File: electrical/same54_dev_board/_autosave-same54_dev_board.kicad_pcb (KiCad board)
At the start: 2 copper layers, 177.8 x 83.8 mm, 7 parts, among them J1 USB_B_Micro, J2 Conn_ARM_JTAG_SWD_10, J3 Conn_02x20_Odd_Even_LCD_INTF, U1 p_ATSAME54P20A-AU, U2 FT232RQ-REEL, U3 MAX7301AAX+, Y1 XOSC32

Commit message: Trying to figure out how I want to do power...
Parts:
- J2: footprint Connector_PinSocket_1.27mm:PinSocket_2x04_P1.27mm_Vertical -> Connector_PinHeader_1.27mm:PinHeader_2x05_P1.27mm_Vertical
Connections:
- net /g_SCREEN_INTF/D0 renamed /s_SCREEN_INTF/D0
- net /g_SCREEN_INTF/D1 renamed /s_SCREEN_INTF/D1
- net /g_SCREEN_INTF/D10 renamed /s_SCREEN_INTF/D10
- net /g_SCREEN_INTF/D11 renamed /s_SCREEN_INTF/D11
- net /g_SCREEN_INTF/D12 renamed /s_SCREEN_INTF/D12
- net /g_SCREEN_INTF/D13 renamed /s_SCREEN_INTF/D13
- net /g_SCREEN_INTF/D14 renamed /s_SCREEN_INTF/D14
- net /g_SCREEN_INTF/D15 renamed /s_SCREEN_INTF/D15
- net /g_SCREEN_INTF/D16 renamed /s_SCREEN_INTF/D16
- net /g_SCREEN_INTF/D17 renamed /s_SCREEN_INTF/D17
- net /g_SCREEN_INTF/D18 renamed /s_SCREEN_INTF/D18
- net /g_SCREEN_INTF/D19 renamed /s_SCREEN_INTF/D19
- net /g_SCREEN_INTF/D2 renamed /s_SCREEN_INTF/D2
- net /g_SCREEN_INTF/D20 renamed /s_SCREEN_INTF/D20
- net /g_SCREEN_INTF/D21 renamed /s_SCREEN_INTF/D21
- net /g_SCREEN_INTF/D22 renamed /s_SCREEN_INTF/D22
- net /g_SCREEN_INTF/D23 renamed /s_SCREEN_INTF/D23
- net /g_SCREEN_INTF/D3 renamed /s_SCREEN_INTF/D3
- net /g_SCREEN_INTF/D4 renamed /s_SCREEN_INTF/D4
- net /g_SCREEN_INTF/D5 renamed /s_SCREEN_INTF/D5
- net /g_SCREEN_INTF/D6 renamed /s_SCREEN_INTF/D6
- net /g_SCREEN_INTF/D7 renamed /s_SCREEN_INTF/D7
- net /g_SCREEN_INTF/D8 renamed /s_SCREEN_INTF/D8
- net /g_SCREEN_INTF/D9 renamed /s_SCREEN_INTF/D9
- net /g_SCREEN_INTF/MASTER_SPI_CLK renamed /s_SCREEN_INTF/MASTER_SPI_CLK
- net /g_SCREEN_INTF/MASTER_SPI_MISO renamed /s_SCREEN_INTF/MASTER_SPI_MISO
- net /g_SCREEN_INTF/MASTER_SPI_MOSI renamed /s_SCREEN_INTF/MASTER_SPI_MOSI
- net /g_SCREEN_INTF/TFT_RSDC renamed /s_SCREEN_INTF/TFT_RSDC
- net /g_SCREEN_INTF/TFT_STB renamed /s_SCREEN_INTF/TFT_STB
- net /g_SCREEN_INTF/TFT_TE renamed /s_SCREEN_INTF/TFT_TE
- net /g_SCREEN_INTF/TFT_TOUCH_INT renamed /s_SCREEN_INTF/TFT_TOUCH_INT
- net /g_SCREEN_INTF/TFT_TOUCH_SCL renamed /s_SCREEN_INTF/TFT_TOUCH_SCL
- net /g_SCREEN_INTF/TFT_TOUCH_SDA renamed /s_SCREEN_INTF/TFT_TOUCH_SDA
- net /g_SCREEN_INTF/~IO_EXPANDER_CS renamed /s_SCREEN_INTF/~IO_EXPANDER_CS
- net /g_SCREEN_INTF/~TFT_CS renamed /s_SCREEN_INTF/~TFT_CS
- net /g_SCREEN_INTF/~TFT_RD renamed /s_SCREEN_INTF/~TFT_RD
- net /g_SCREEN_INTF/~TFT_RST renamed /s_SCREEN_INTF/~TFT_RST
- net /g_SCREEN_INTF/~TFT_WR renamed /s_SCREEN_INTF/~TFT_WR
- J1 pad 1: Net-(J1-Pad1) -> g_5v
- J1 pad 5: Net-(J1-Pad5) -> GND
- J1 pad 6: Net-(J1-Pad6) -> GND
- U1 pad 25: Net-(U1-Pad25) -> Net-(U1-Pad14)
- U2 pad 1: Net-(U2-Pad1) -> /s_USB_INTF.sch/3v3_Enable
- U2 pad 16: Net-(U2-Pad16) -> /s_USB_INTF.sch/3v3_Enable
- U2 pad 17: Net-(U2-Pad17) -> GND
- U2 pad 19: Net-(U2-Pad19) -> g_5v
- U2 pad 20: Net-(U2-Pad20) -> GND
- U2 pad 24: Net-(U2-Pad24) -> GND
- U2 pad 26: Net-(U2-Pad26) -> GND
- U2 pad 33: Net-(U2-Pad33) -> GND
- U2 pad 4: Net-(U2-Pad4) -> GND
- U2 pad 9: Net-(U2-Pad9) -> /s_USB_INTF.sch/3v3_Enable

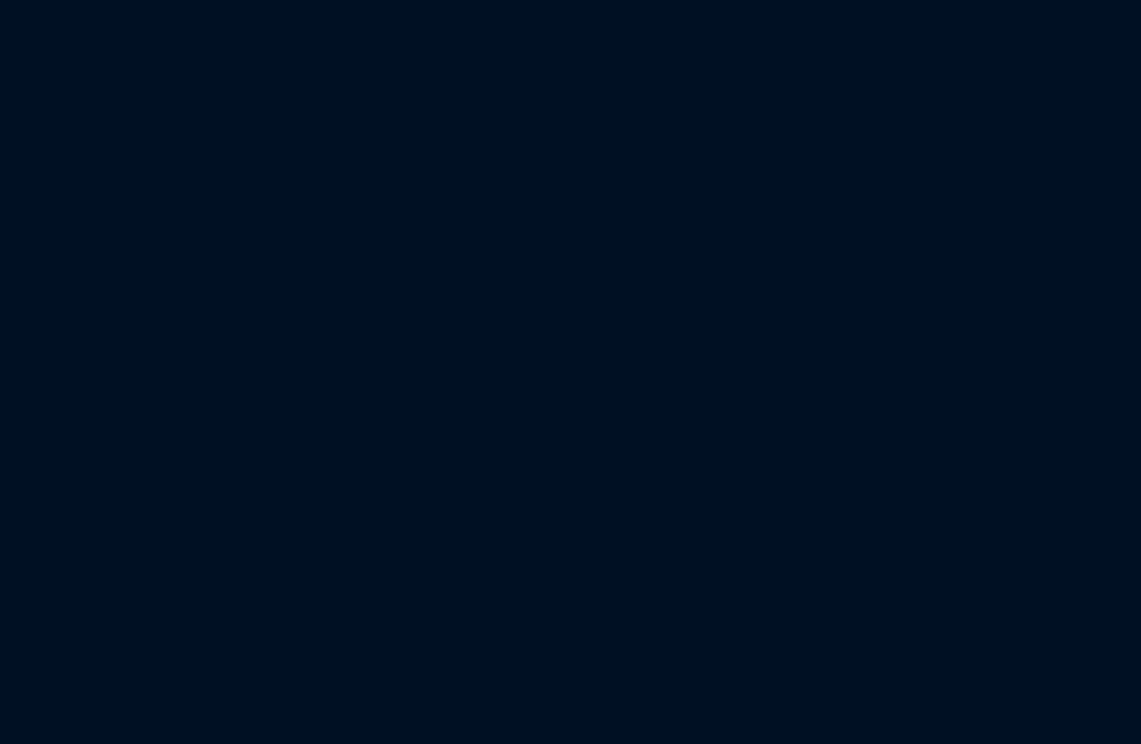
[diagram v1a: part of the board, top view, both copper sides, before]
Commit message: Added usart, i2c, and spi pin locations, as well as labeled sercoms
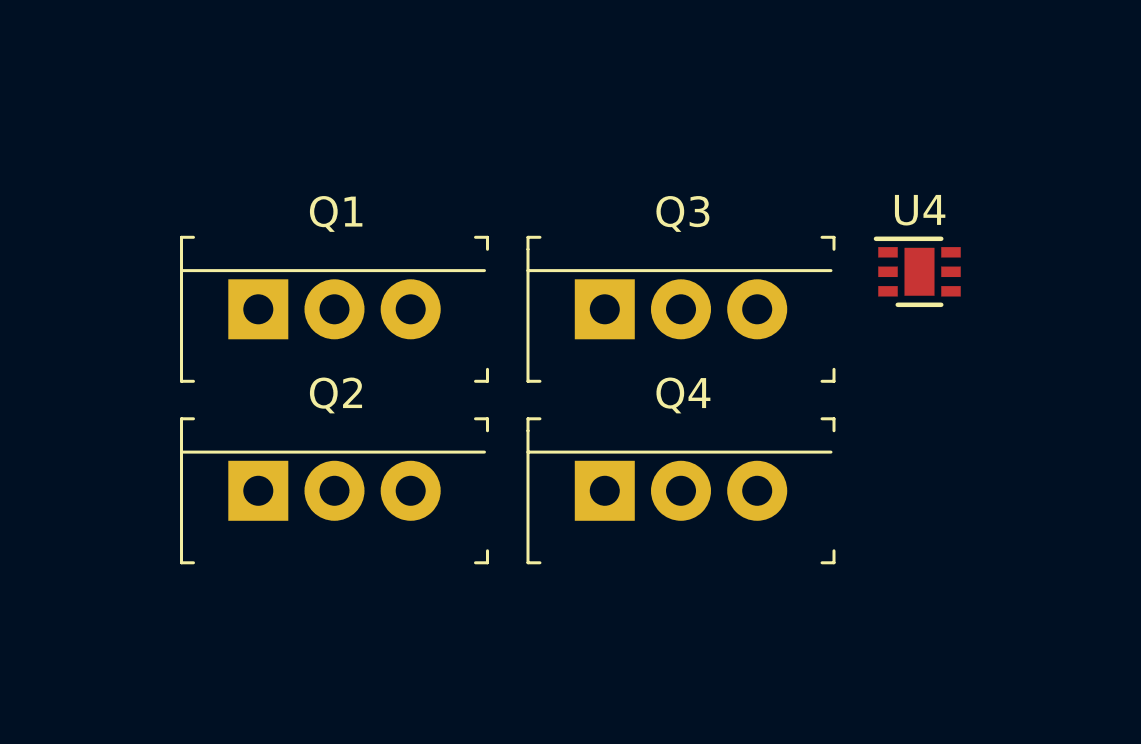
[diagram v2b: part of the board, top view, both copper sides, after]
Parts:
- added Q1: Default PFET_A, digikey-footprints:TO-220-3, F.Cu at (137.2, 82.5)
- added Q2: Alt PFET_A, digikey-footprints:TO-220-3, F.Cu at (137.2, 88.6)
- added Q3: Default PFET_B, digikey-footprints:TO-220-3, F.Cu at (148.7, 82.5)
- added Q4: Alt PFET_B, digikey-footprints:TO-220-3, F.Cu at (148.7, 88.6)
- added U4: NCP349MNAETBG, Package_DFN_QFN:DFN-6-1EP_2x2mm_P0.65mm_EP1x1.6mm, F.Cu at (159.2, 81.3)
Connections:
- net /s_SCREEN_INTF/MASTER_SPI_MOSI renamed /MASTER_SPI_MOSI
- net /s_SCREEN_INTF/~TFT_CS renamed /~TFT_CS
- net /s_USB_INTF.sch/3v3_Enable renamed /s_USB_INTF.sch/FTDI_3V3
- J1 pad 1: g_5v -> Net-(C7-Pad1)
- J3 pad 3: /s_SCREEN_INTF/TFT_TOUCH_SCL -> /MASTER_I2C_SCL
- J3 pad 4: /s_SCREEN_INTF/TFT_TOUCH_SDA -> /MASTER_I2C_SDA
- U1 pad 100: Net-(U1-Pad100) -> /DEBUG_RX
- U1 pad 101: Net-(U1-Pad101) -> /DEBUG_TX
- U1 pad 118: Net-(U1-Pad118) -> Net-(U1-Pad107)
- U1 pad 21: Net-(U1-Pad21) -> /MASTER_SPI_MISO
- U1 pad 22: Net-(U1-Pad22) -> /MASTER_SPI_CLK
- U1 pad 23: Net-(U1-Pad23) -> /MASTER_SPI_MISO
- U1 pad 46: Net-(U1-Pad46) -> Net-(U1-Pad107)
- U1 pad 54: Net-(U1-Pad54) -> Net-(U1-Pad107)
- U1 pad 65: Net-(U1-Pad65) -> Net-(U1-Pad107)
- U1 pad 66: Net-(U1-Pad66) -> /MASTER_I2C_SDA
- U1 pad 67: Net-(U1-Pad67) -> /MASTER_I2C_SCL
- U1 pad 79: Net-(U1-Pad79) -> Net-(U1-Pad107)
- U1 pad 91: Net-(U1-Pad91) -> Net-(U1-Pad107)
- U1 pad 97: Net-(U1-Pad97) -> Net-(U1-Pad107)
- U2 pad 19: g_5v -> /s_USB_INTF.sch/FTDI_5V
- U3 pad 33: /s_SCREEN_INTF/MASTER_SPI_CLK -> /MASTER_SPI_CLK
- U3 pad 4: /s_SCREEN_INTF/MASTER_SPI_MISO -> /MASTER_SPI_MISO
